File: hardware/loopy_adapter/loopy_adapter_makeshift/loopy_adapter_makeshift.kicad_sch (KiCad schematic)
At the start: 6 parts, among them J1 CART SLOT TOP ROW, J2 CART SLOT BOTTOM ROW, J3 CART SLOT TOP ROW, J4 CART SLOT BOTTOM ROW, J5 Loopy_Cart_Side, J6 Loopy_Cart_Side

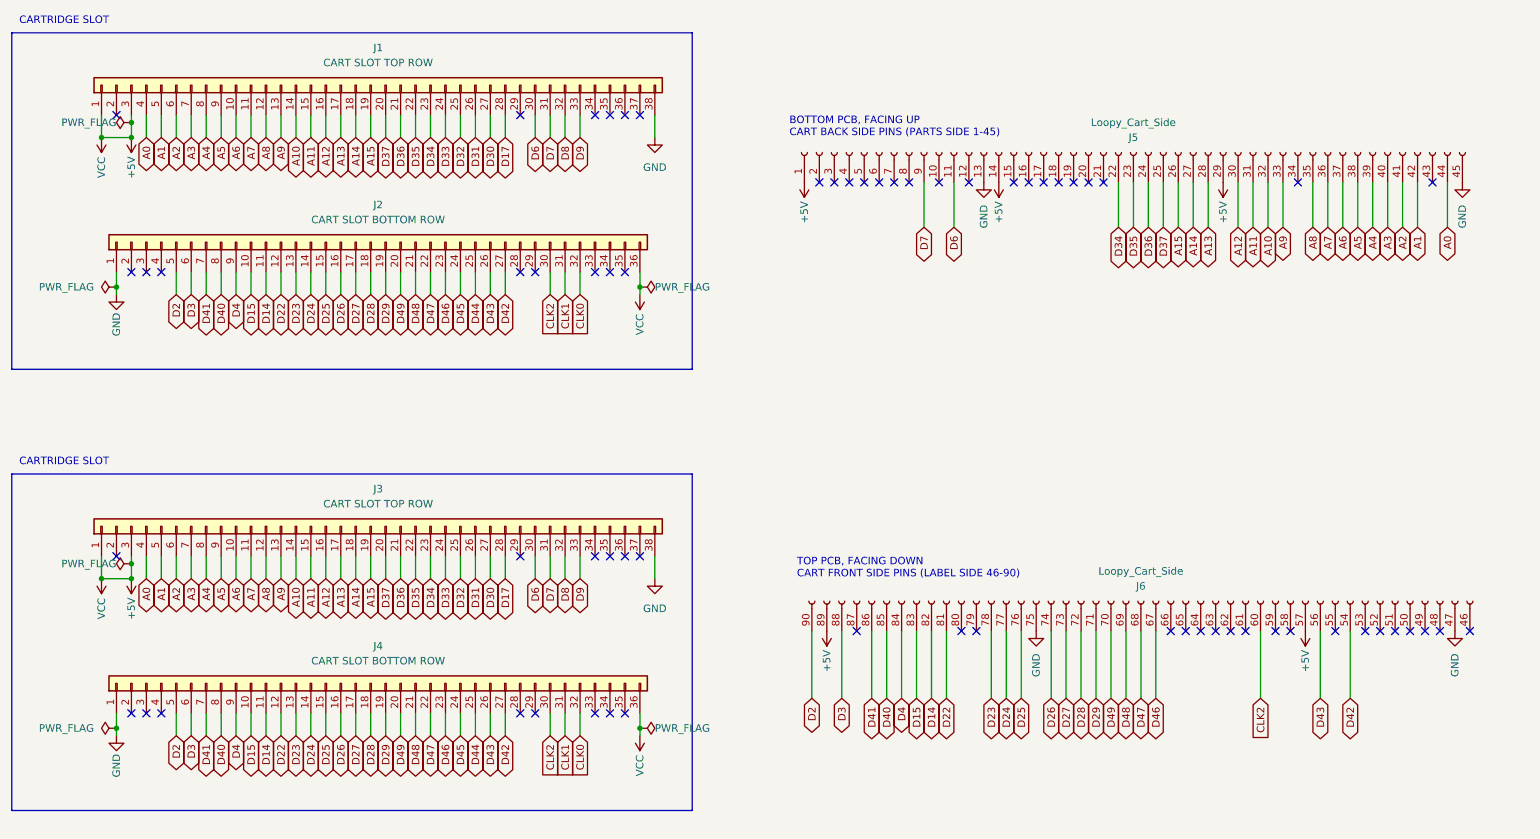
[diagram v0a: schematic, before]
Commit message: Sandwiching spring contacts between top and bottom for removability
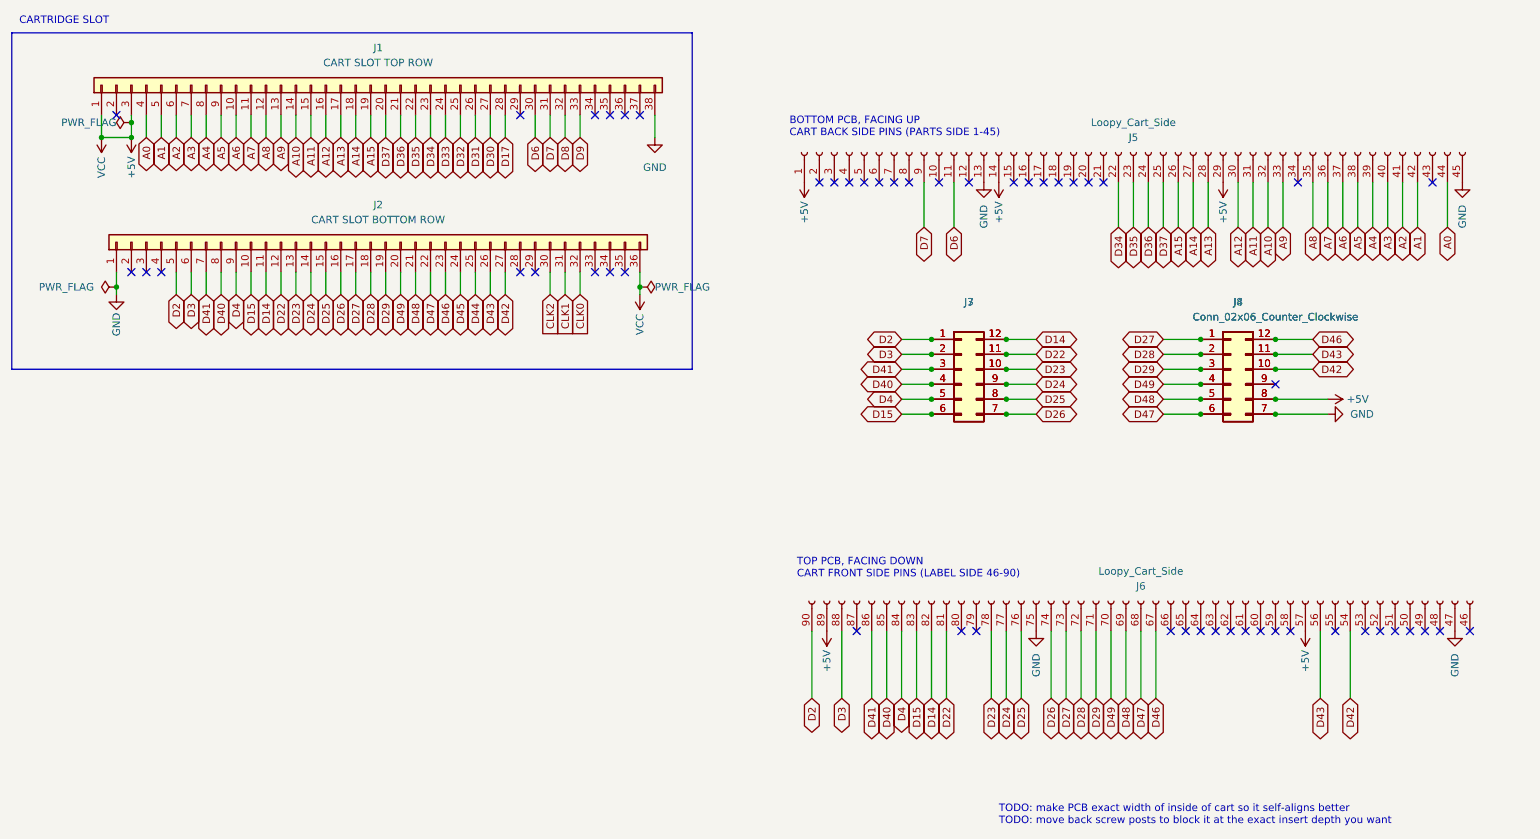
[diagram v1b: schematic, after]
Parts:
- removed J3: CART SLOT TOP ROW, Connector_PinSocket_2.54mm:PinSocket_1x38_P2.54mm_Vertical, symbol Connector_Generic:Conn_01x38
- removed J4: CART SLOT BOTTOM ROW, Connector_PinSocket_2.54mm:PinSocket_1x36_P2.54mm_Vertical, symbol Connector_Generic:Conn_01x36
- added J3, J4: Conn_02x06_Counter_Clockwise, OSCR:Loopy_Makeshift_SpringContacts_M_THT_02x06, symbol Connector_Generic:Conn_02x06_Counter_Clockwise
- added J7, J8: Conn_02x06_Counter_Clockwise, OSCR:Loopy_Makeshift_SpringContacts_F_SMD_Pad_02x06, symbol Connector_Generic:Conn_02x06_Counter_Clockwise
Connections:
- net +5V: now also J4.8 (Pin_8), J8.8 (Pin_8)
- net CLK2: no longer J6.60
- net D14: now also J3.12 (Pin_12), J7.12 (Pin_12)
- net D15: now also J3.6 (Pin_6), J7.6 (Pin_6)
- net D2: now also J3.1 (Pin_1), J7.1 (Pin_1)
- net D22: now also J3.11 (Pin_11), J7.11 (Pin_11)
- net D23: now also J3.10 (Pin_10), J7.10 (Pin_10)
- net D24: now also J3.9 (Pin_9), J7.9 (Pin_9)
- net D25: now also J3.8 (Pin_8), J7.8 (Pin_8)
- net D26: now also J3.7 (Pin_7), J7.7 (Pin_7)
- net D27: now also J4.1 (Pin_1), J8.1 (Pin_1)
- net D28: now also J4.2 (Pin_2), J8.2 (Pin_2)
- net D29: now also J4.3 (Pin_3), J8.3 (Pin_3)
- net D3: now also J3.2 (Pin_2), J7.2 (Pin_2)
- net D4: now also J3.5 (Pin_5), J7.5 (Pin_5)
- net D40: now also J3.4 (Pin_4), J7.4 (Pin_4)
- net D41: now also J3.3 (Pin_3), J7.3 (Pin_3)
- net D42: now also J4.10 (Pin_10), J8.10 (Pin_10)
- net D43: now also J4.11 (Pin_11), J8.11 (Pin_11)
- net D46: now also J4.12 (Pin_12), J8.12 (Pin_12)
- net D47: now also J4.6 (Pin_6), J8.6 (Pin_6)
- net D48: now also J4.5 (Pin_5), J8.5 (Pin_5)
- net D49: now also J4.4 (Pin_4), J8.4 (Pin_4)
- net GND: now also J4.7 (Pin_7), J8.7 (Pin_7)
- new net: J4.9 (Pin_9), J8.9 (Pin_9)
- no-connect marks 65 -> 53
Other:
- note added: "TODO: make PCB exact width of inside of cart so it self-aligns better TODO: move back screw posts to block it at the exact insert depth you want"
